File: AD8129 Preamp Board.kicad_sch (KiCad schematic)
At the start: 9 parts

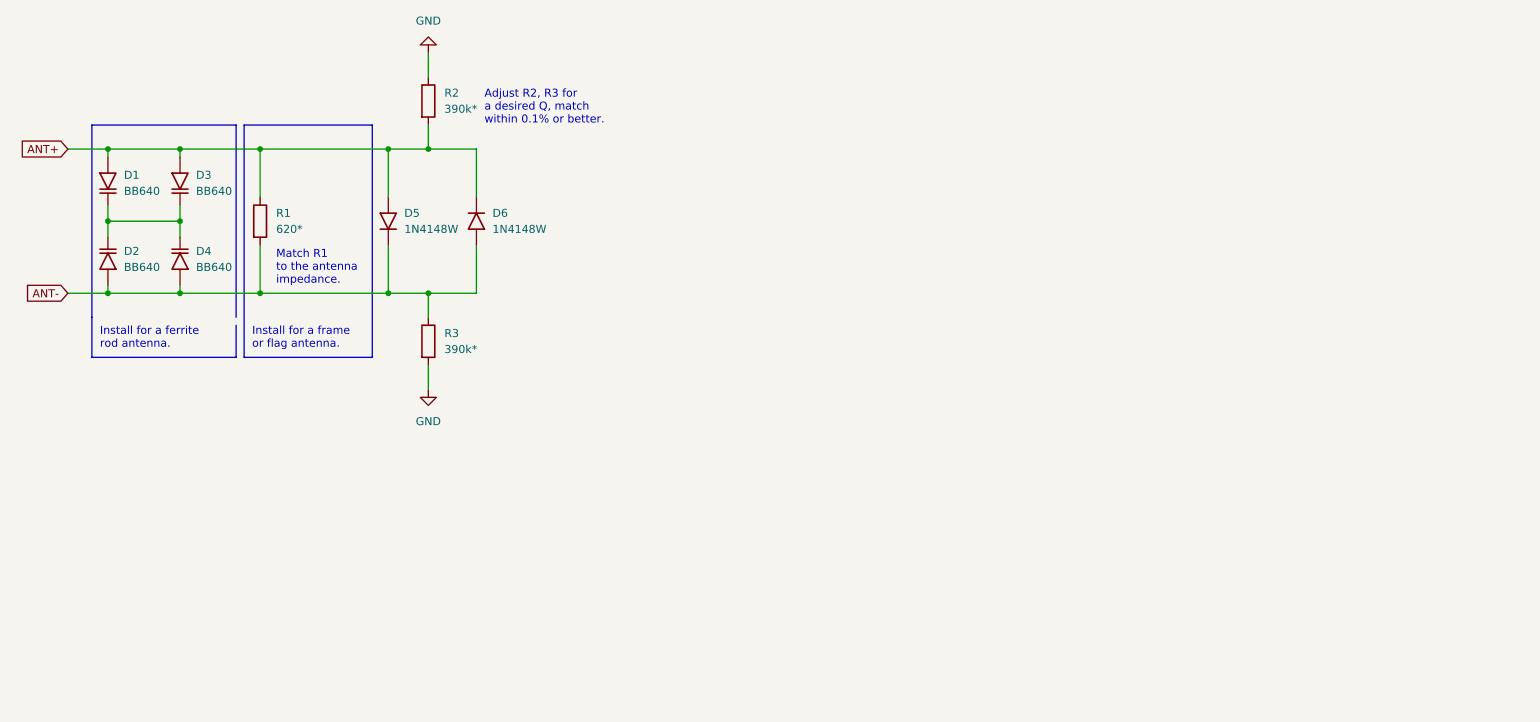
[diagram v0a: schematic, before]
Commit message: ADD: preamp w/o varicap control
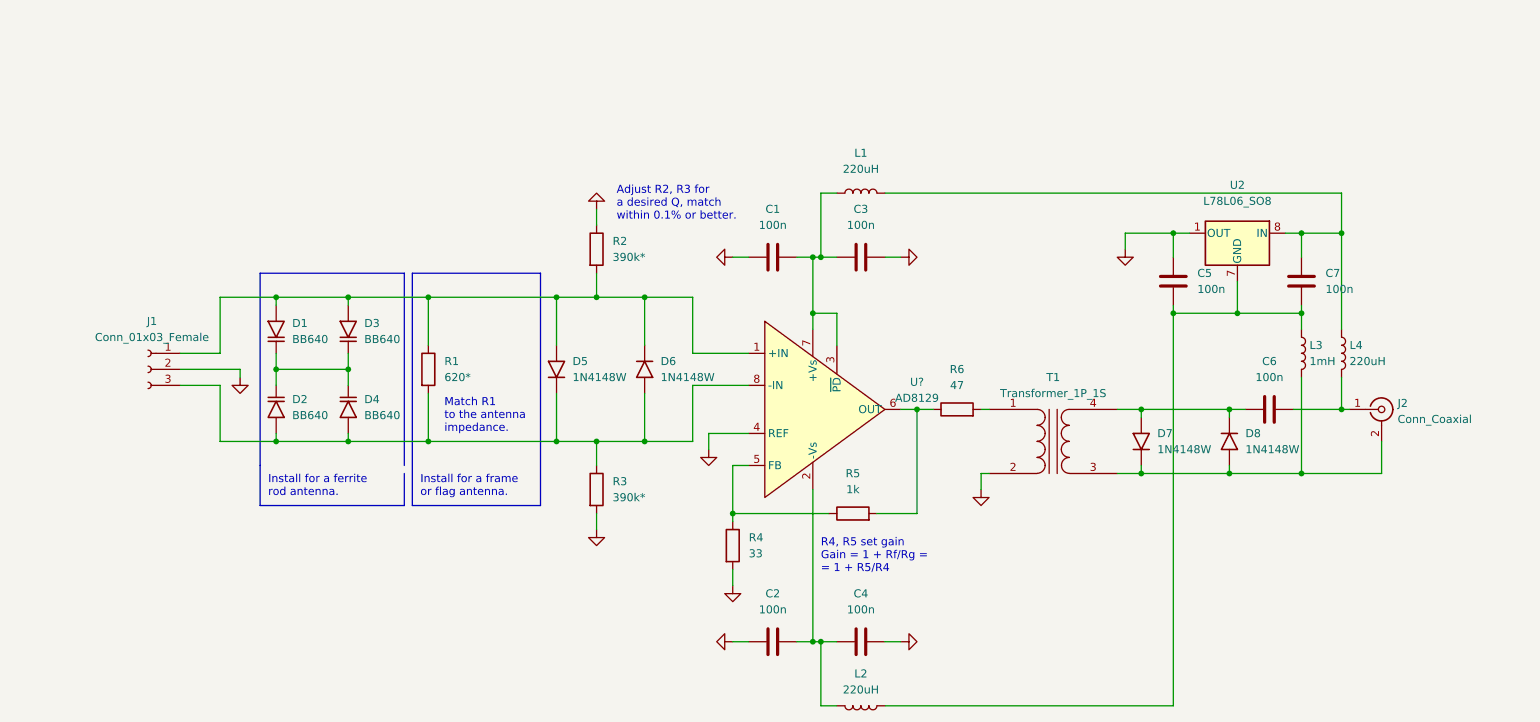
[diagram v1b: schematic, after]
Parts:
- added C1, C2, C3, C4, C5, C6, C7: 100n, symbol AD8129 Preamp Board:C
- added D7, D8: 1N4148W, symbol AD8129 Preamp Board:D
- added J1: Conn_01x03_Female, symbol AD8129 Preamp Board:Conn_01x03_Female
- added J2: Conn_Coaxial, symbol AD8129 Preamp Board:Conn_Coaxial
- added L1, L2, L4: 220uH, symbol AD8129 Preamp Board:L
- added L3: 1mH, symbol AD8129 Preamp Board:L
- added R4: 33, symbol AD8129 Preamp Board:R
- added R5: 1k, symbol AD8129 Preamp Board:R
- added R6: 47, symbol AD8129 Preamp Board:R
- added T1: Transformer_1P_1S, symbol AD8129 Preamp Board:Transformer_1P_1S
- added U2: L78L06_SO8, Package_SO:SOIC-8_3.9x4.9mm_P1.27mm, symbol AD8129 Preamp Board:L78L06_SO8
- added U?: AD8129, symbol AD8129 Preamp Board:AD8129
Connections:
- net GND: now also C1.1, C2.2, C3.2, C4.1, C5.1, J1.2 (Pin_2), R4.2, T1.2 (AB), U2.1 (OUT), U?.4 (REF)
- net ANT+: no longer names the net of D1.2 (A), D3.2 (A), D5.2 (A), D6.1 (K), R1.1, R2.2
- net ANT+: now also J1.1 (Pin_1), U?.1 (+IN)
- net ANT-: no longer names the net of D2.2 (A), D4.2 (A), D5.1 (K), D6.2 (A), R1.2, R3.1
- net ANT-: now also J1.3 (Pin_3), U?.8 (-IN)
- new net: C5.2, C7.2, L2.1, L3.1, U2.2 (GND), U2.3 (GND), U2.6 (GND), U2.7 (GND)
- new net: C7.1, L1.2, L4.1, U2.8 (IN)
- new net: D7.1 (K), D8.2 (A), J2.2 (Ext), L3.2, T1.3 (SA)
- new net: C6.1, D7.2 (A), D8.1 (K), T1.4 (SB)
- new net: C2.1, C4.2, L2.2, U?.2 (-Vs)
- new net: C1.2, C3.1, L1.1, U?.3 (~{PD}), U?.7 (+Vs)
- new net: R4.1, R5.1, U?.5 (FB)
- new net: R5.2, R6.1, U?.6 (OUT)
- new net: C6.2, J2.1 (In), L4.2
- new net: R6.2, T1.1 (AA)
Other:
- note added: "R4, R5 set gain Gain = 1 + Rf/Rg = = 1 + R5/R4"
- moved on the sheet: D1, D2, D3, D4, D5, D6, R1, R2, R3

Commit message: ADD: tuning block, complete schematics, unverified
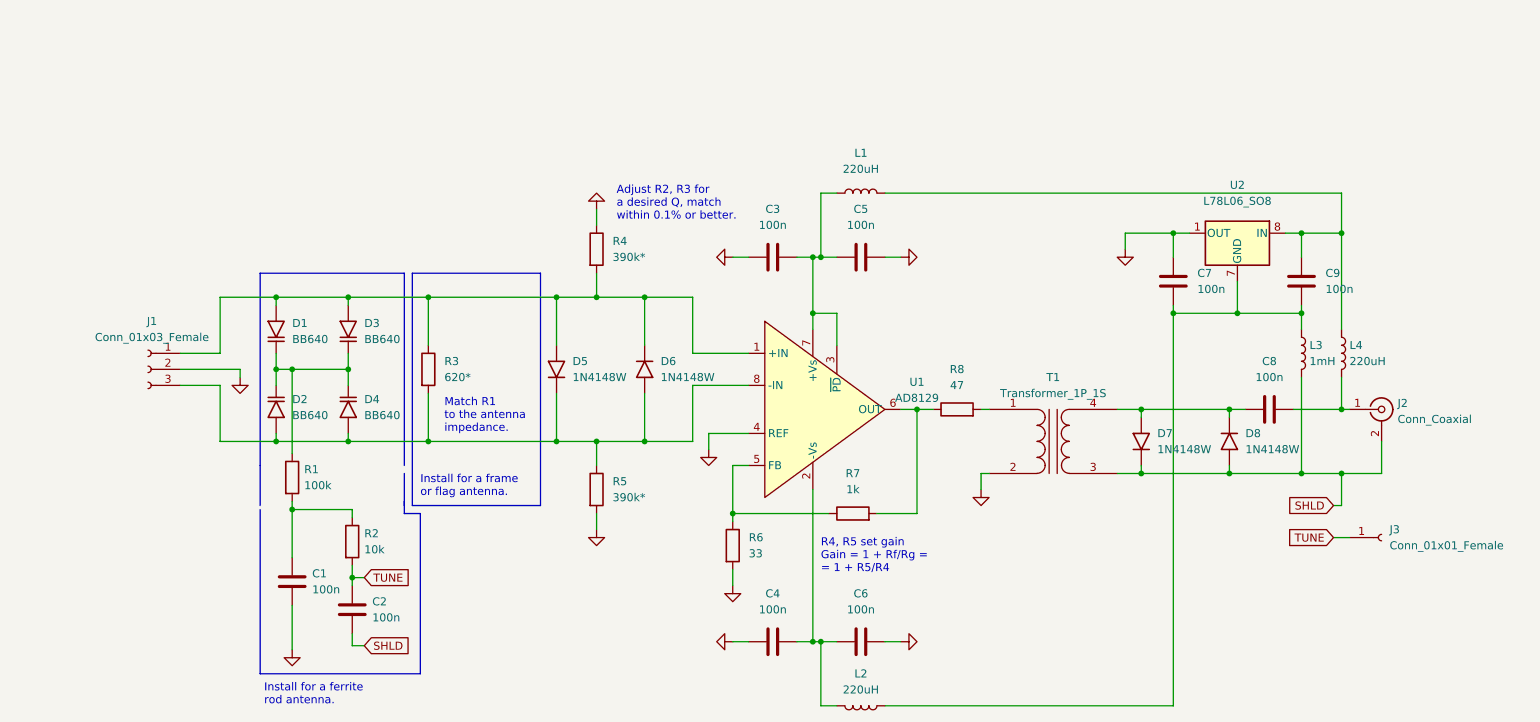
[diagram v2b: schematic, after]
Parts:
- added C1, C2: 100n, symbol AD8129 Preamp Board:C
- added J3: Conn_01x01_Female, symbol AD8129 Preamp Board:Conn_01x01_Female
- added R1: 100k, symbol AD8129 Preamp Board:R
- added R2: 10k, symbol AD8129 Preamp Board:R
- gave numbers to parts that had none: 1
- renumbered C1 to C3, C2 to C4, C3 to C5, C4 to C6, C5 to C7, C6 to C8, C7 to C9, R1 to R3, R2 to R4, R3 to R5, R4 to R6, R5 to R7, R6 to R8
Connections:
- net GND: now also C1.2
- net SHLD: now reaches D7.1 (K), D8.2 (A), J2.2 (Ext), L3.2, T1.3 (SA)
- net SHLD: now also C2.2
- net at D1.1 (K), D2.1 (K), D3.1 (K)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: now also R1.1
- new net: C1.1, R1.2, R2.1
- new net TUNE: C2.1, J3.1 (Pin_1), R2.2
